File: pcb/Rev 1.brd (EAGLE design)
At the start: 76.8 x 76.8 mm, 218 parts, among them J1 3220-10-0100-00, J2 10118194-0001LF, J3 B2B-PH-K-S(LF)(SN), Q1 MMBT3904,215MMBT3904,215, Q12 MMBT3904,215MMBT3904,215, Q13 MMBT3904,215MMBT3904,215, Q14 MMBT3904,215MMBT3904,215, Q15 MMBT3904,215MMBT3904,215, Q16 TEFT4300, Q17 TEFT4300, Q18 TEFT4300, Q19 TEFT4300, Q20 MMBT3904,215MMBT3904,215, Q21 MMBT3904,215MMBT3904,215, Q22 MMBT3904,215MMBT3904,215, Q23 MMBT3904,215MMBT3904,215, Q24 TEFT4300, Q25 TEFT4300, Q26 TEFT4300, Q27 TEFT4300, Q28 SI7157DP, Q29 SI7157DP, Q30 MMBT3906, Q31 MMBT3906, Q32 SI7157DP, Q33 MMBT3906, Q34 MMBT3906, U1 ATSAMD21G18A-MU, U10 DRV8871, U11 PCAL6416A, U12 MAX7315, U2 AP3441, U3 TPS61089, U4 BNO055, U5 MCP73811, U7 DRV8871, U8 DRV8871, U9 DRV8871

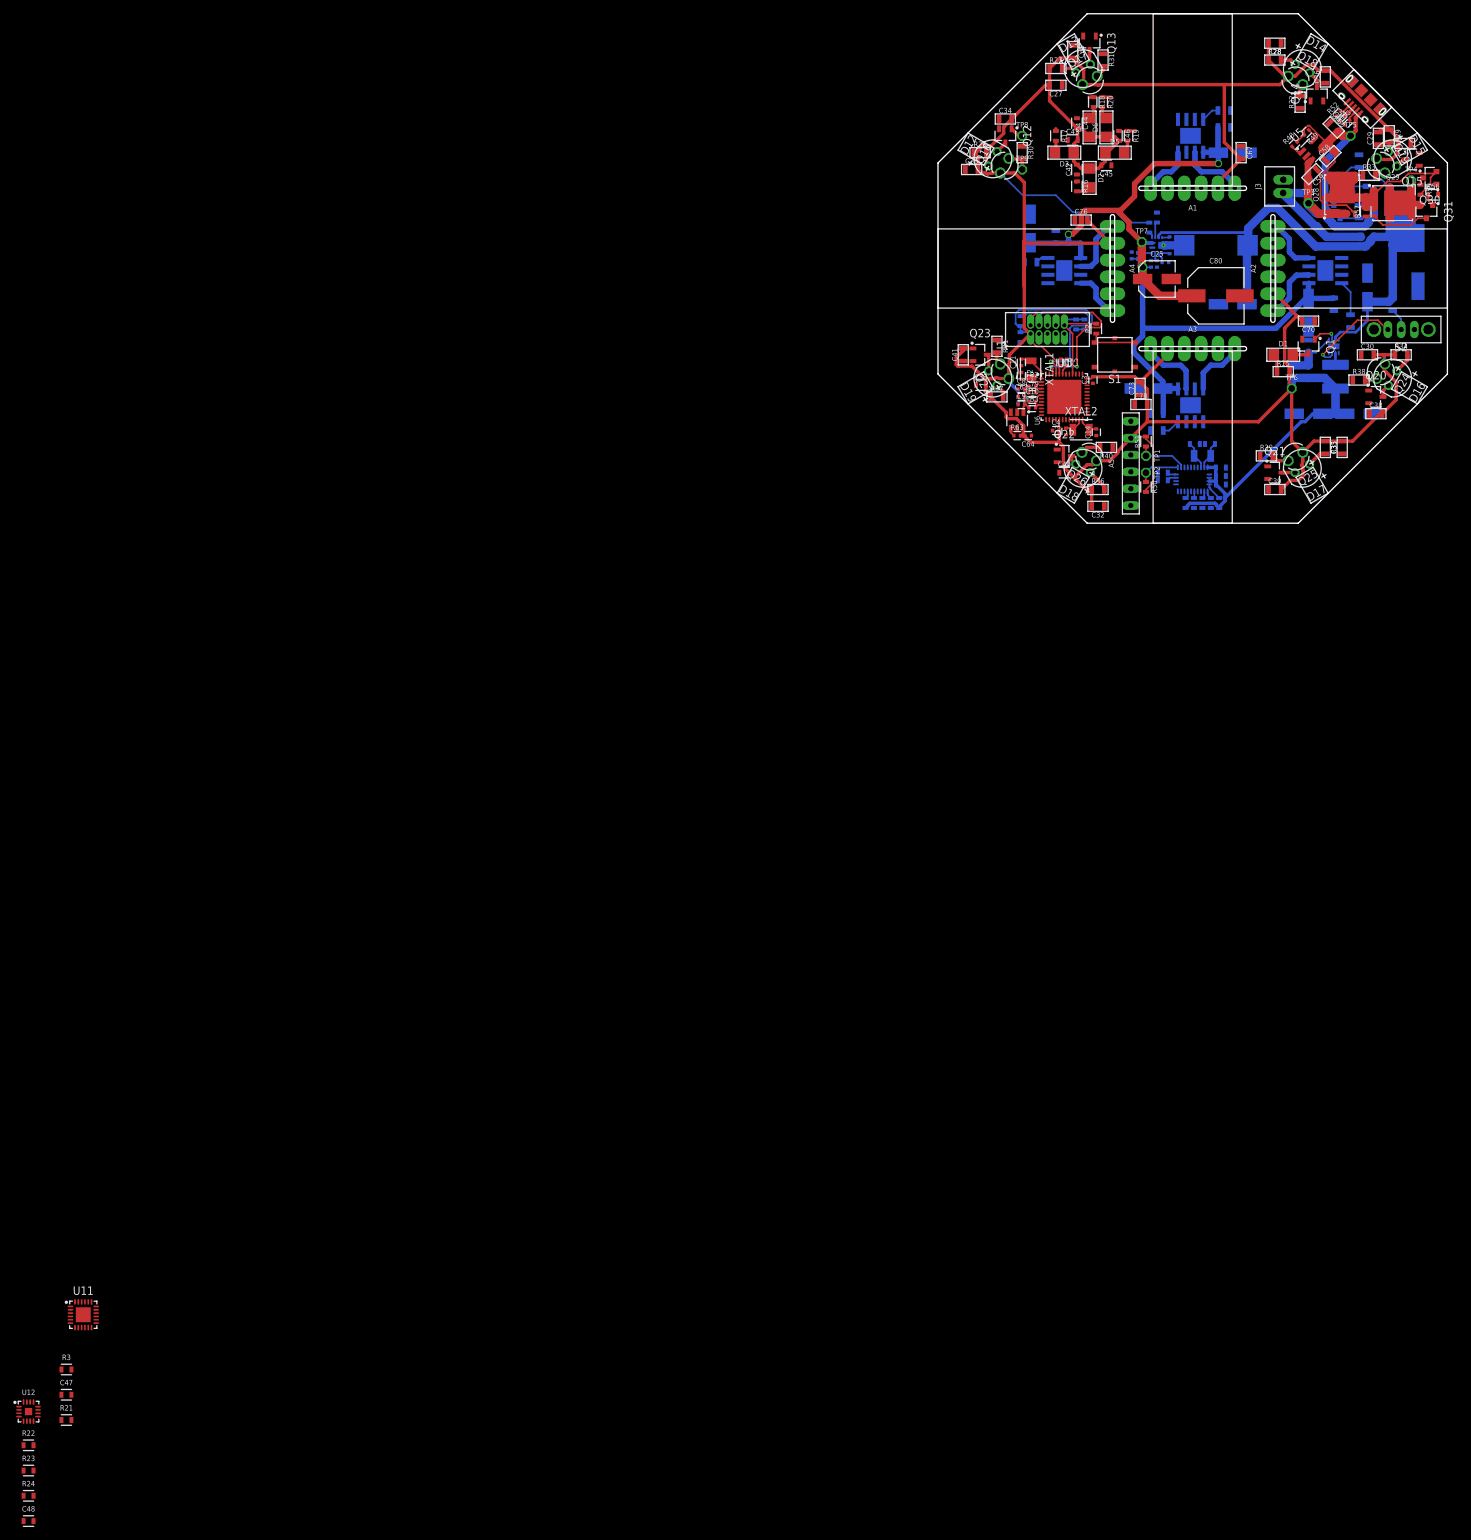
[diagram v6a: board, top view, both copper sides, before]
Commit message: Placed and routed IO expanders
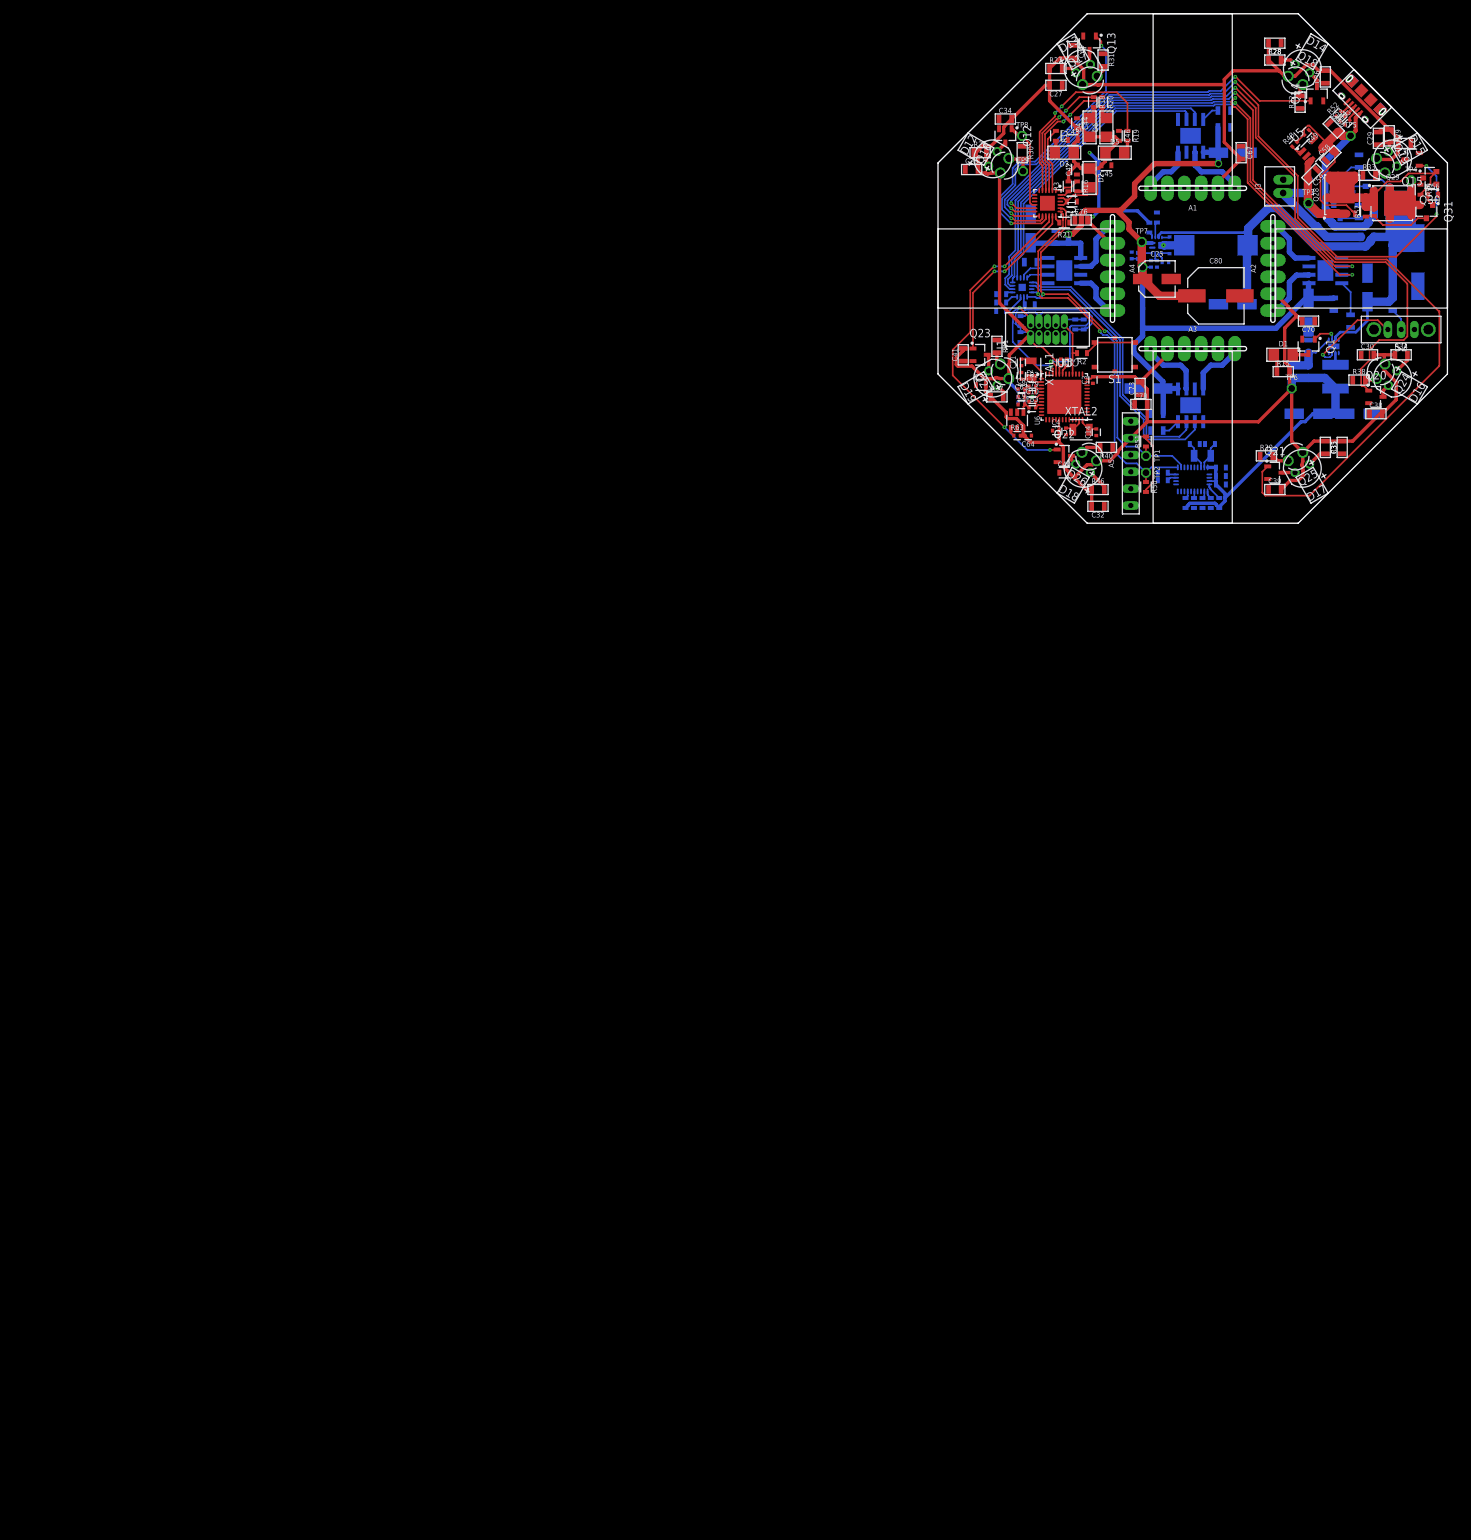
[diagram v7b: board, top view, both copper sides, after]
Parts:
- moved C48 237.7 mm to (13.8, 33.0), flipped to the bottom
- moved C47 235.3 mm to (20.2, 48.5), turned to 180 degrees
- moved R21 235.1 mm to (19.1, 45.3), turned to 180 degrees
- moved R3 233.8 mm to (19.7, 50.8), turned to 90 degrees
- moved R24 231.2 mm to (9.53, 32.0), flipped to the bottom, turned to 180 degrees
- moved R23 229.2 mm to (9.53, 33.3), flipped to the bottom, turned to 180 degrees
- moved R22 227.3 mm to (9.53, 34.5), flipped to the bottom, turned to 180 degrees
- moved U12 226.3 mm to (12.7, 35.6), flipped to the bottom, turned to 180 degrees
- moved U11 221.9 mm to (16.5, 48.3), turned to 270 degrees
- moved R2 4.27 mm to (21.7, 25.7), turned to 180 degrees
- moved TP9 0.28 mm to (12.8, 53.1)
- moved C7 0.13 mm to (20.7, 30.0)
- moved R1 0.13 mm to (22.0, 30.0)
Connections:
- net IR2: now also U11.15; no longer U11.11
- net IR3: now also U11.14; no longer U11.12
- net IR5: now also U11.11; no longer U11.14
- net IR6: now also U11.12; no longer U11.15
- net LED2: now also U11.4; no longer U11.3
- net LED3: now also U11.5; no longer U11.4
- net LED4: now also U11.3; no longer U11.5
- net MOTOR_1A: now also U12.4; no longer U12.2
- net MOTOR_1B: now also U12.5; no longer U12.3
- net MOTOR_2A: now also U12.2; no longer U12.4
- net MOTOR_2B: now also U12.3; no longer U12.5
- net MOTOR_3A: now also U12.9; no longer U12.7
- net MOTOR_3B: now also U12.10; no longer U12.8
- net MOTOR_4A: now also U12.7; no longer U12.9
- net MOTOR_4B: now also U12.8; no longer U12.10
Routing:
- net IR6: track 0.00 -> 145.2 mm, vias 0 -> 2
- net IR5: track 0.00 -> 110.6 mm, vias 0 -> 2
- net IR4: track 0.00 -> 108.6 mm, vias 0 -> 4
- net MOTOR_2A: track 0.00 -> 91.6 mm, vias 0 -> 2
- net MOTOR_2B: track 0.00 -> 87.8 mm, vias 0 -> 2
- net IR3: track 0.00 -> 66.0 mm, vias 0 -> 2
- net SCL: track 6.53 -> 59.1 mm, vias 0 -> 2
- net SDA: track 7.66 -> 59.8 mm, vias 0 -> 2
- net IR7: track 0.00 -> 51.4 mm, vias 0 -> 4
- net MOTOR_1A: track 0.00 -> 46.0 mm
- net IR2: track 0.00 -> 43.7 mm, vias 0 -> 2
- net MOTOR_1B: track 0.00 -> 43.1 mm
- net MOTOR_3B: track 0.00 -> 42.5 mm
- net MOTOR_3A: track 0.00 -> 41.1 mm
- net LED3: track 1.19 -> 29.9 mm, vias 0 -> 2
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
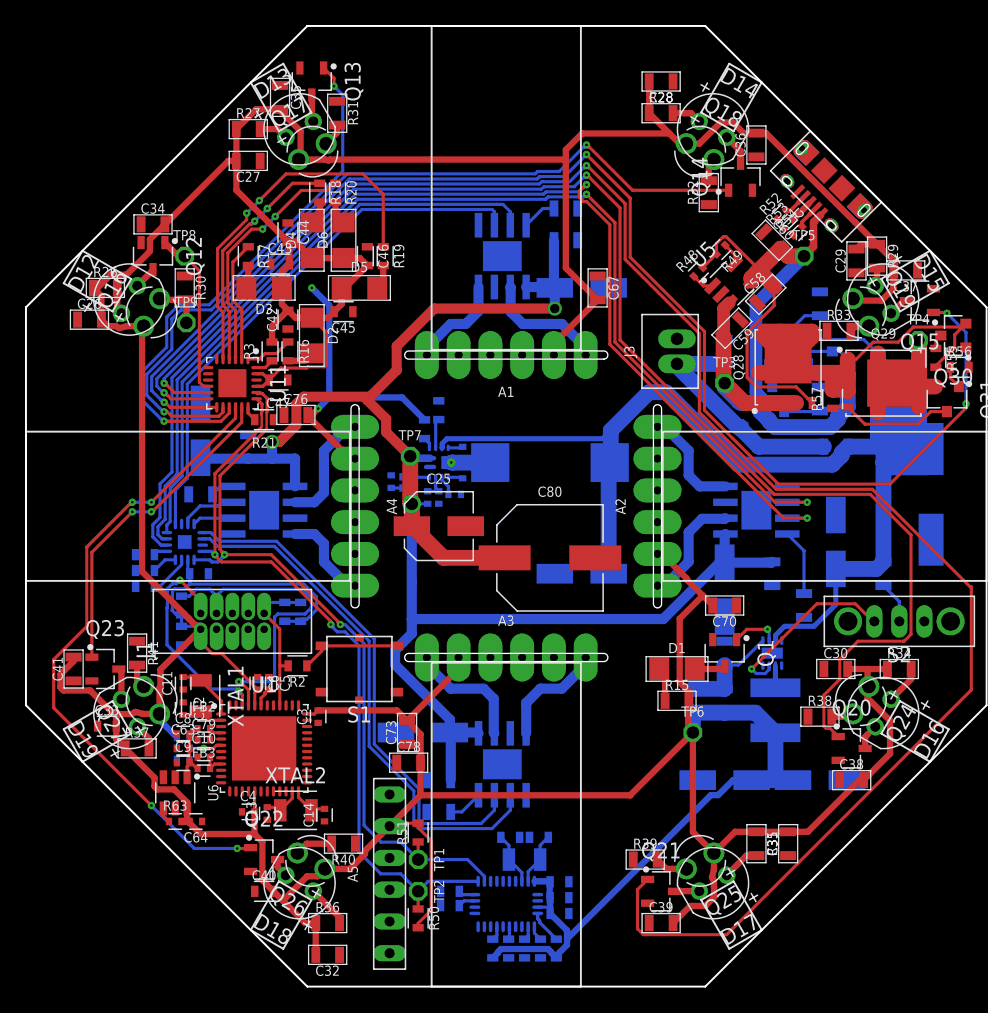
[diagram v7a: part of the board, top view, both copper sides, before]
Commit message: Finished routing signals to MCU
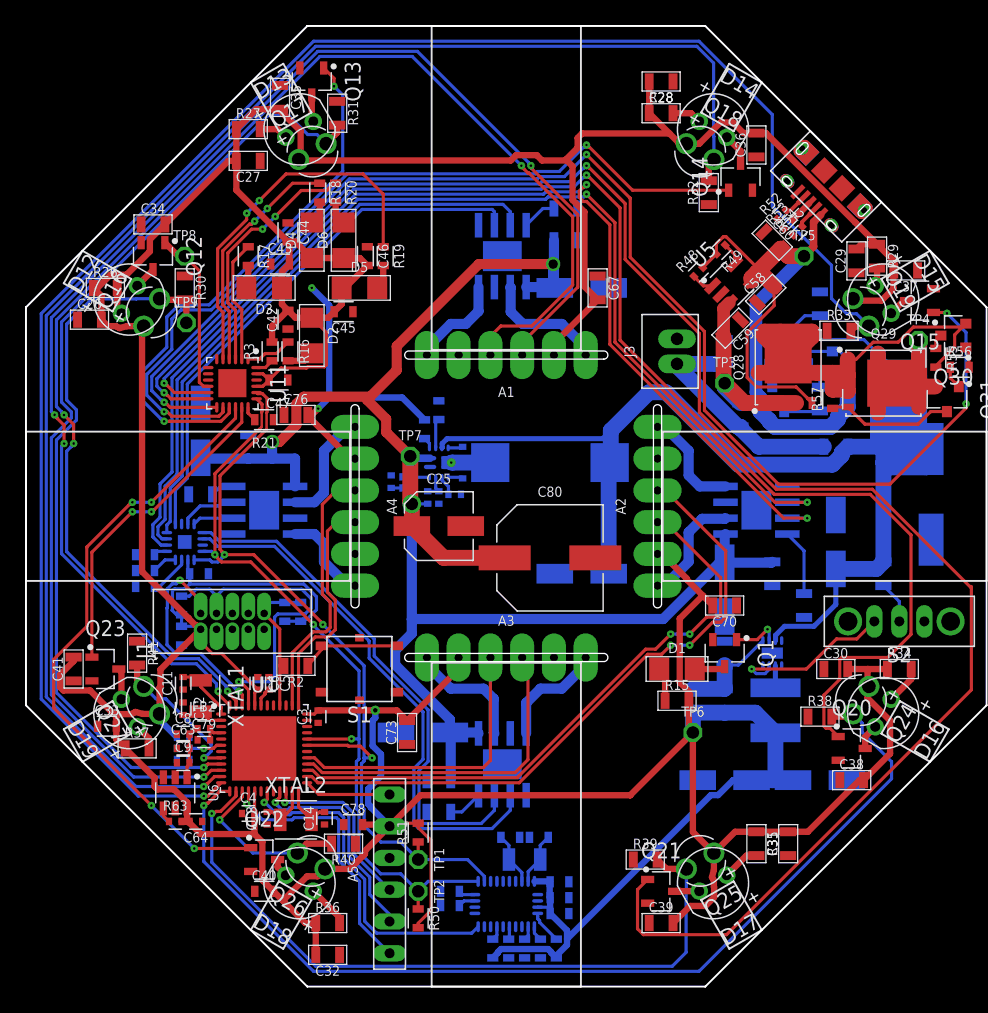
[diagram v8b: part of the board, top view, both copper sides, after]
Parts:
- removed C10: 0.1uF, Micromouse 2020:0402
- removed FB3: (no value), Micromouse 2020:0402
- C78: device Micromouse 2020:0805 -> Micromouse 2020:0603
- R2: device Micromouse 2020:0603 -> Micromouse 2020:0805
- moved C78 6.66 mm to (26.2, 13.0)
- moved XTAL2 0.76 mm to (21.6, 13.3)
- moved C13 0.38 mm to (19.3, 13.5)
- moved C14 0.25 mm to (23.9, 13.5)
- moved C4 0.13 mm to (17.8, 13.8)
- moved R2 0.13 mm to (21.6, 25.7)
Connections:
- removed net VREFB: C10.2, FB3.2, U1.9
- net !RESET: now also R2.P$2; no longer R2.2
- net +3V3: now also C78.2; no longer C78.P$2
- net BT_EN: now also U1.25
- net BT_RX: now also U1.22
- net BT_STATE: now also U1.16
- net BT_TX: now also U1.21
- net ENCODER_1A: now also U1.48
- net ENCODER_1B: now also U1.47
- net ENCODER_2A: now also U1.27
- net ENCODER_2B: now also U1.26
- net ENCODER_3A: now also U1.29
- net ENCODER_3B: now also U1.28
- net ENCODER_4A: now also U1.38
- net ENCODER_4B: now also U1.37
- net GND: now also C78.1; no longer C10.1, C78.P$1
- net IMU_INT: now also U1.19
- net N$1: now also R2.P$1; no longer R2.1
- net N$999: no longer FB3.1
- net PHOTO1: now also U1.9
- net PHOTO2: now also U1.10
- net PHOTO3: now also U1.11
- net PHOTO4: now also U1.12
- net PHOTO5: now also U1.13
- net PHOTO6: now also U1.14
- net PHOTO7: now also U1.15
- net PHOTO8: now also U1.8
- net SCL: now also U1.32
- net SDA: now also U1.31
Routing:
- net PHOTO4: track 1.59 -> 141.0 mm, vias 0 -> 1
- net PHOTO3: track 1.86 -> 120.2 mm, vias 0 -> 1
- net ENCODER_1B: track 0.00 -> 109.0 mm, vias 0 -> 4
- net ENCODER_1A: track 0.00 -> 107.8 mm, vias 0 -> 4
- net PHOTO5: track 1.78 -> 80.3 mm, vias 0 -> 1
- net PHOTO2: track 1.85 -> 78.1 mm, vias 0 -> 1
- net PHOTO6: track 2.65 -> 58.0 mm, vias 0 -> 1
- net PHOTO1: track 3.95 -> 58.5 mm, vias 0 -> 1
- net ENCODER_2B: track 0.00 -> 51.9 mm, vias 0 -> 2
- net ENCODER_2A: track 0.00 -> 48.6 mm, vias 0 -> 2
- net ENCODER_3B: track 0.00 -> 26.7 mm
- net IMU_INT: track 0.00 -> 26.7 mm, vias 0 -> 1
- net ENCODER_3A: track 0.00 -> 23.4 mm
- net BT_STATE: track 0.00 -> 21.5 mm, vias 0 -> 1
- net ENCODER_4A: track 0.00 -> 21.3 mm
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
